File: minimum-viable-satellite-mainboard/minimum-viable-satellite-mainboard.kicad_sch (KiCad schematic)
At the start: 50 parts, among them J1 Breakout, J2 Breakout, Q1 FDMQ86530L, Q2 DMP2240UDM-7, Q3 DMP2240UDM-7, U1 TLV1704

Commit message: More Schematic Capture
- Moved WDT to its own sheet
- Added Solar Charger
- Added MCP Temp Sensor
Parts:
- removed C1, C2, C3, C4, C5: 10u, Capacitor_SMD:C_0603_1608Metric, symbol Device:C_Small
- removed D1, D3: 1N4151WS, Diode_SMD:D_SOD-323, symbol oresat-diodes:1N4151WS-HE3
- removed D2: GREEN, LED_SMD:LED_0603_1608Metric, symbol Device:LED_Small_Filled
- removed J1: Breakout, Connector_PinHeader_2.54mm:PinHeader_1x04_P2.54mm_Vertical, symbol Connector_Generic:Conn_01x04
- removed J2: Breakout, FC_DEV_BOARD:JST_BM04B-SRSS-TB(LF)(SN), symbol Connector_Generic:Conn_01x04
- removed JP1: SolderJumper_2_Open, Jumper:SolderJumper-2_P1.3mm_Open_RoundedPad1.0x1.5mm, symbol Jumper:SolderJumper_2_Open
- removed R1: 10 (1206), Resistor_SMD:R_1206_3216Metric, symbol Device:R_Small_US
- removed R10, R12: 1k, Resistor_SMD:R_0603_1608Metric, symbol Device:R_Small_US
- removed R11, R13, R14, R15, R17, R18: 100k, Resistor_SMD:R_0603_1608Metric, symbol Device:R_Small_US
- removed R16: 4.7M, Resistor_SMD:R_0603_1608Metric, symbol Device:R_Small_US
- removed R2, R3, R4, R8, R9: 10k, Resistor_SMD:R_0603_1608Metric, symbol Device:R_Small_US
- removed R5, R6, R7: 3.0k, Resistor_SMD:R_0603_1608Metric, symbol Device:R_Small_US
- removed TP1, TP2, TP3, TP4, TP5, TP6: TestPoint-MinTH, oresat-misc:TestPoint-0.75mm-th, symbol oresat-misc:Test-Point-0.75mm-th
- removed U1: TLV1704, Package_SO:TSSOP-14_4.4x5mm_P0.65mm, symbol oresat-ics:TLV1704AIPWR
- added C10, C8: 10uF, Capacitor_SMD:C_0603_1608Metric, symbol mainboard:10UF-0603-6.3V-20%
- added C6, C7: 0.1uF, Capacitor_SMD:C_0603_1608Metric, symbol Device:C_Small
- added C9: 1uF, Capacitor_SMD:C_0603_1608Metric, symbol mainboard:10UF-0603-6.3V-20%
- added D10, D8: DFLS130L, Diode_SMD:D_PowerDI-123, symbol Device:D_Schottky
- added D5, D6, D7, D9: DFLS130L-7, Diode_SMD:D_PowerDI-123, symbol Device:D_Schottky
- added IC1: LT3652IMSE#PBF, Package_SO:MSOP-12-1EP_3x4mm_P0.65mm_EP1.65x2.85mm, symbol LT3652IMSE#PBF:LT3652IMSE#PBF
- added J3: Foot0, Battery Board:MOLEX_504050-0291, symbol Connector_Generic:Conn_01x02
- added J4: Foot1, Battery Board:MOLEX_504050-0291, symbol Connector_Generic:Conn_01x02
- added J5, J9: ISS Foot0, Battery Board:MOLEX_504050-0291, symbol Connector_Generic:Conn_01x02
- added J6: Foot2, Battery Board:MOLEX_504050-0291, symbol Connector_Generic:Conn_01x02
- added J7: Foot3, Battery Board:MOLEX_504050-0291, symbol Connector_Generic:Conn_01x02
- added J8: RBF Pin, Battery Board:MOLEX_504050-0291, symbol Connector_Generic:Conn_01x04
- added L1: 10uH, Inductor_SMD:L_1812_4532Metric, symbol Device:L
- added R25, R26, R35, R36: 0.002, Resistor_SMD:R_2512_6332Metric, symbol mainboard:R-US_R2512
- added R27: 100K, Resistor_SMD:R_0603_1608Metric, symbol Device:R_US
- added R28: 100k, Resistor_SMD:R_0603_1608Metric, symbol mainboard:R-US_R0603
- added R29: 94k, Resistor_SMD:R_0603_1608Metric, symbol mainboard:R-US_R0603
- added R30, R34: 10K, Resistor_SMD:R_0603_1608Metric, symbol Device:R_US
- added R31: 634k, Resistor_SMD:R_0603_1608Metric, symbol mainboard:R-US_R0603
- added R32: 412k, Resistor_SMD:R_0603_1608Metric, symbol mainboard:R-US_R0603
- added R33: 0.1, Resistor_SMD:R_2512_6332Metric, symbol mainboard:R-US_R0603
- added U2, U3: INA219AxD, Package_SO:SOIC-8_3.9x4.9mm_P1.27mm, symbol Analog_ADC:INA219AxD
- added U4: MCP9808_MSOP, Package_SO:MSOP-8_3x3mm_P0.65mm, symbol Sensor_Temperature:MCP9808_MSOP
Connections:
- net GND: now also C10.2, C6.1, C7.1, C8.2, D9.2 (A), IC1.13 (EP), IC1.6 (TIMER), J5.1 (Pin_1), J9.1 (Pin_1), R29.1, R32.1, R35.1, R36.1, U2.2 (A0), U2.6 (GND), U3.1 (A1), U3.2 (A0), U3.6 (GND), U4.4 (GND)
- new net: IC1.2 (VIN_REG), R28.2, R29.2
- new net: C8.1, D5.1 (K), D6.1 (K), IC1.1 (VIN), IC1.3 (~{SHDN}), R27.1
- new net: R27.2, R28.1
- new net: J6.1 (Pin_1), J7.2 (Pin_2)
- new net: C9.1, D9.1 (K), IC1.12 (SW), L1.1
- new net: C9.2, D8.1 (K), IC1.11 (BOOST)
- new net: J3.1 (Pin_1), J4.2 (Pin_2)
- new net: IC1.10 (SENSE), L1.2, R33.2
- new net: IC1.7 (VFB), R31.1, R32.2
- new net +3V3: C6.2, C7.2, R30.1, R34.1, U2.1 (A1), U2.5 (VS), U3.5 (VS), U4.8 (V_{DD})
- new net Dir_Chrg_In: D6.2 (A), D7.2 (A)
- new net PACK+: R26.2, U3.8 (IN+)
- new net PACK-: J5.2 (Pin_2), J9.2 (Pin_2), R35.2, R36.2
- new net SCL0: U2.4 (SCL), U3.4 (SCL)
- new net SDA0: U2.3 (SDA), U3.3 (SDA)
- new net VBATT_SENSE: C10.1, D10.2 (A), D8.2 (A), IC1.9 (BAT), R26.1, R31.2, R33.1, U3.7 (IN-)
- new net VBUSP: J8.1 (Pin_1), J8.2 (Pin_2)
- new net VBatt: D10.1 (K), D7.1 (K), J3.2 (Pin_2), J6.2 (Pin_2)
- new net VBatt1: J4.1 (Pin_1), J7.1 (Pin_1), J8.3 (Pin_3), J8.4 (Pin_4)
- new net VSOLAR_IN: D5.2 (A), R25.2, U2.8 (IN+)
- new net VSOLAR_OUT: R25.1, U2.7 (IN-)
- new net ~{CHRG}: IC1.4 (~{CHRG}), R30.2
- new net ~{FAULT}: IC1.5 (~{FAULT}), R34.2
- no-connect marks 4 -> 5
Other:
- added sheet Watchdog Timer (watchdog.kicad_sch)
- note added: "2S Li-Ion Battery Solar Charging Circuit"
- note added: "Battery Power Monitor"
- note added: "Current Sense Resistor: 2mOhm suggested on datasheet"
- note added: "Schottky Diode"
- note added: "Solar Power Monitor"
- note added: "Temperature Sensor"
- note added: "VSOLAR 9V to 40V"
- note removed: "C112+C114 and R62+R63 set the WDT frequency"
- note removed: "DC block and pulse detector"
- note removed: "Disable shutdown during initial power up."
- note removed: "OreSat Watch-Dog Timer"
- note removed: "Oscillator"
- note removed: "Output buffer"
- note removed: "Pull-up on battery pack to Vbus"
- note removed: "Pulse integrator"
- note removed: "TLV1704AMPWPSEP is the radiation tolerant version. Use TLV1704AQPWRQ1 for non-flight C3 boards."
- note removed: "WDT enabled when soldered"
- note removed: "~ 24 s period (36 s on power up)"
- moved on the sheet: D4, Q1, Q2A, Q2B, Q3A, Q3B, R19, R20, R21, R22, R23, R24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

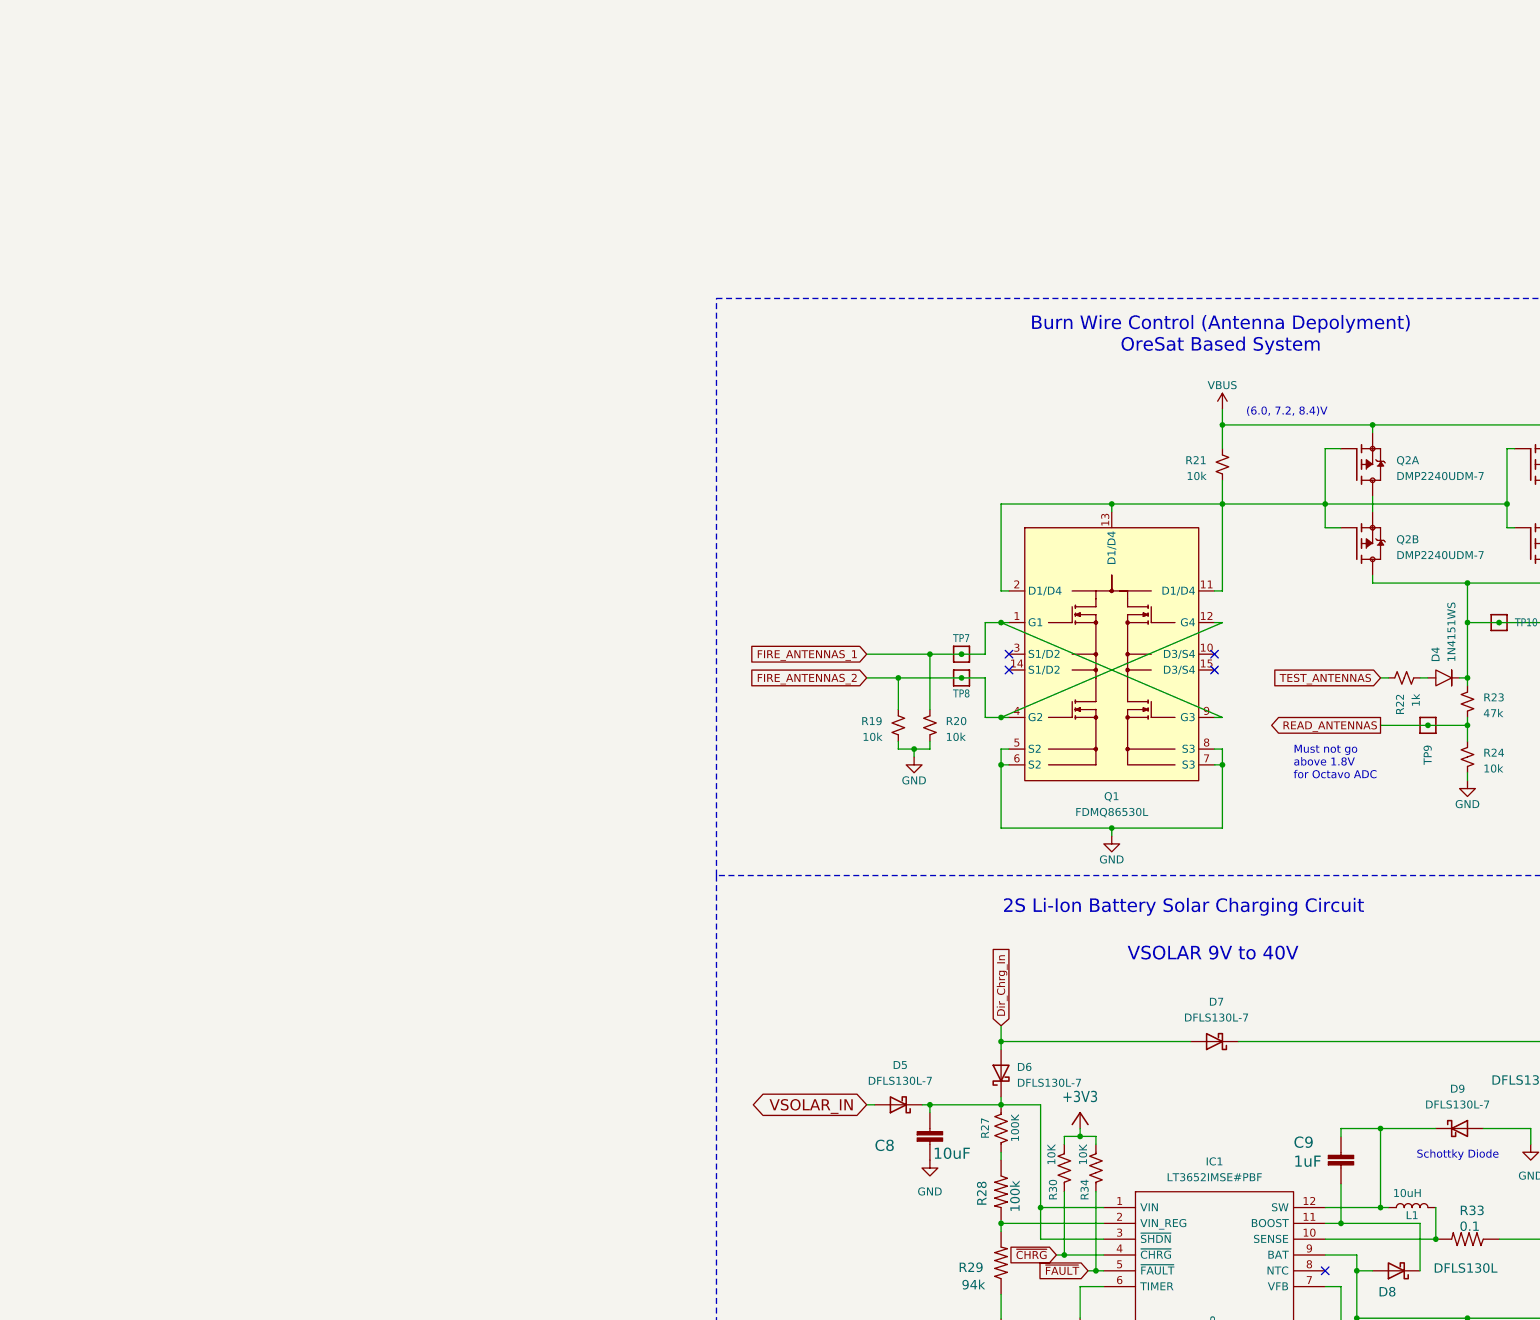
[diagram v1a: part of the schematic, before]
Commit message: added MSP430
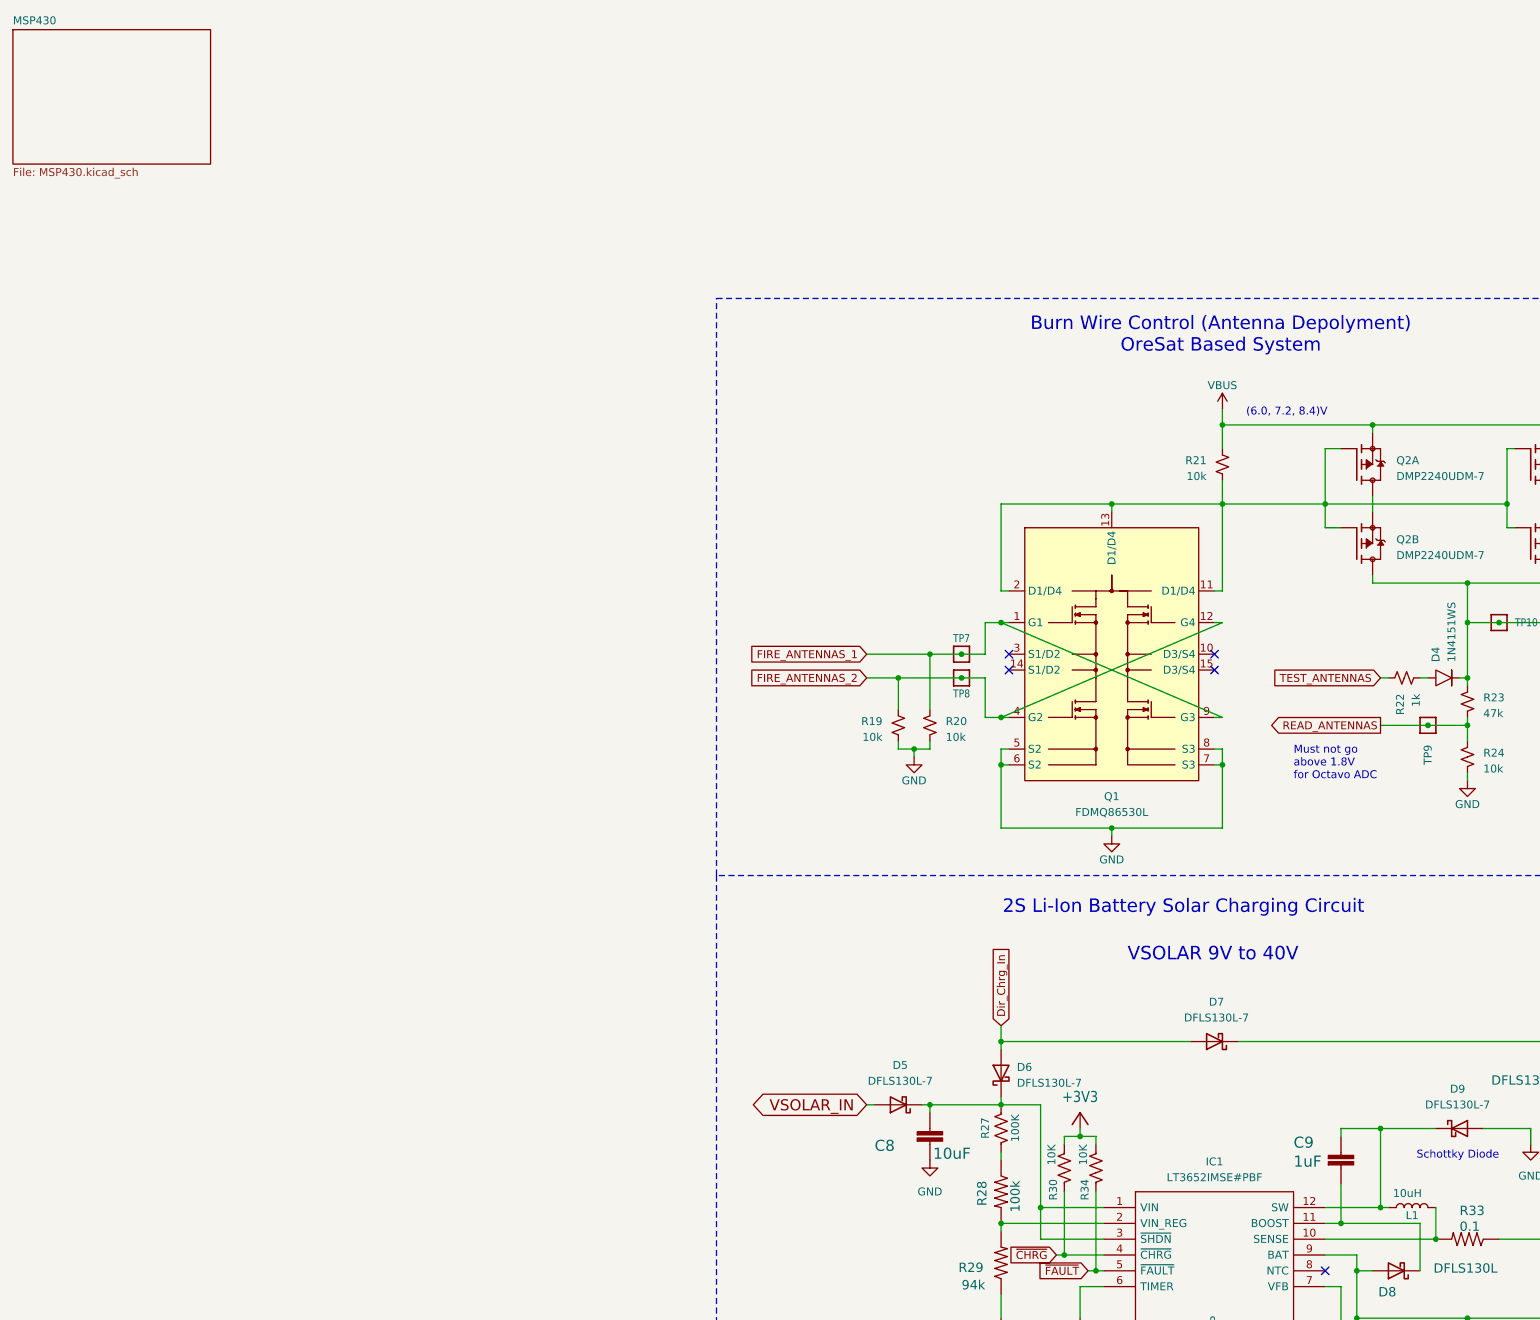
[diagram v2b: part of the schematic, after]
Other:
- added sheet MSP430 (MSP430.kicad_sch)
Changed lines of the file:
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@@
 (kicad_sch
-	(version 20231120)
+	(version 20250114)
 	(generator "eeschema")
-	(generator_version "8.0")
+	(generator_version "9.0")
 	(paper "A3")
+	(text "2S Li-Ion Battery Solar Charging Circuit"
+		(exclude_from_sim no)
+		(at 179.324 161.29 0)
+		(effects
+			(font
+				(size 2.159 2.159)
+			)
+			(justify left bottom)
+		)
+	)
+	(text "Current Sense Resistor:\n2mOhm suggested on datasheet\n"
+		(exclude_from_sim no)
+		(at 311.15 181.61 0)
+		(effects
+			(font
+				(size 0.889 0.889)
+			)
+			(justify left bottom)
+		)
+	)
+	(text "Current Sense Resistor:\n2mOhm suggested on datasheet\n"
+		(exclude_from_sim no)
+		(at 313.69 221.488 0)
+		(effects
+			(font
+				(size 0.889 0.889)
+			)
+			(justify left bottom)
+		)
+	)
+	(text "Must not go \nabove 1.8V \nfor Octavo ADC"
+		(exclude_from_sim no)
+		(at 226.06 139.7 0)
+		(effects
+			(font
+				(size 1.27 1.27)
+			)
+			(justify left bottom)
+		)
+	)
+	(text "Battery Power Monitor"
+		(exclude_from_sim no)
+		(at 349.25 206.248 0)
+		(effects
+			(font
+				(size 2.159 2.159)
+			)
+			(justify left bottom)
+		)
+	)
+	(text "Schottky Diode\n"
+		(exclude_from_sim no)
+		(at 259.08 200.66 0)
+		(effects
+			(font
+				(size 1.27 1.27)
+			)
+			(justify right bottom)
+		)
+	)
+	(text "VSOLAR 9V to 40V"
+		(exclude_from_sim no)
+		(at 199.39 168.91 0)
+		(effects
+			(font
+				(size 2.159 2.159)
+			)
+			(justify left bottom)
+		)
+	)
+	(text "Solar Power Monitor"
+		(exclude_from_sim no)
+		(at 346.71 165.608 0)
+		(effects
+			(font
+				(size 2.159 2.159)
+			)
+			(justify left bottom)
+		)
+	)
+	(text "Burn Wire Control (Antenna Depolyment)\nOreSat Based System"
+		(exclude_from_sim no)
+		(at 214.376 71.12 0)
+		(effects
+			(font
+				(size 2.159 2.159)
+			)
+			(justify bottom)
+		)
+	)
+	(text "(6.0, 7.2, 8.4)V"
+		(exclude_from_sim no)
+		(at 218.44 81.28 0)
+		(effects
+			(font
+				(size 1.27 1.27)
+			)
+			(justify left bottom)
+		)
+	)
+	(text "Temperature Sensor\n"
+		(exclude_from_sim no)
+		(at 357.124 83.312 0)
+		(effects
+			(font
+				(size 1.27 1.27)
+			)
+		)
+	)
 	(junction
 		(at 167.64 191.77)
@@
 		)
 	)
-	(text "2S Li-Ion Battery Solar Charging Circuit"
-		(exclude_from_sim no)
-		(at 179.324 161.29 0)
-		(effects
-			(font
-				(size 2.159 2.159)
-			)
-			(justify left bottom)
-		)
-	)
-	(text "Current Sense Resistor:\n2mOhm suggested on datasheet\n"
-		(exclude_from_sim no)
-		(at 311.15 181.61 0)
-		(effects
-			(font
-				(size 0.889 0.889)
-			)
-			(justify left bottom)
-		)
-	)
-	(text "Current Sense Resistor:\n2mOhm suggested on datasheet\n"
-		(exclude_from_sim no)
-		(at 313.69 221.488 0)
-		(effects
-			(font
-				(size 0.889 0.889)
-			)
-			(justify left bottom)
-		)
-	)
-	(text "Must not go \nabove 1.8V \nfor Octavo ADC"
-		(exclude_from_sim no)
-		(at 226.06 139.7 0)
-		(effects
-			(font
-				(size 1.27 1.27)
-			)
-			(justify left bottom)
-		)
-	)
-	(text "Battery Power Monitor"
-		(exclude_from_sim no)
-		(at 349.25 206.248 0)
-		(effects
-			(font
-				(size 2.159 2.159)
-			)
-			(justify left bottom)
-		)
-	)
-	(text "Schottky Diode\n"
-		(exclude_from_sim no)
-		(at 259.08 200.66 0)
-		(effects
-			(font
-				(size 1.27 1.27)
-			)
-			(justify right bottom)
-		)
-	)
-	(text "VSOLAR 9V to 40V"
-		(exclude_from_sim no)
-		(at 199.39 168.91 0)
-		(effects
-			(font
-				(size 2.159 2.159)
-			)
-			(justify left bottom)
-		)
-	)
-	(text "Solar Power Monitor"
-		(exclude_from_sim no)
-		(at 346.71 165.608 0)
-		(effects
-			(font
-				(size 2.159 2.159)
-			)
-			(justify left bottom)
-		)
-	)
-	(text "Burn Wire Control (Antenna Depolyment)\nOreSat Based System"
-		(exclude_from_sim no)
-		(at 214.376 71.12 0)
-		(effects
-			(font
-				(size 2.159 2.159)
-			)
-			(justify bottom)
-		)
-	)
-	(text "(6.0, 7.2, 8.4)V"
-		(exclude_from_sim no)
-		(at 218.44 81.28 0)
-		(effects
-			(font
-				(size 1.27 1.27)
-			)
-			(justify left bottom)
-		)
-	)
-	(text "Temperature Sensor\n"
-		(exclude_from_sim no)
-		(at 357.124 83.312 0)
-		(effects
-			(font
-				(size 1.27 1.27)
-			)
-		)
-	)
 	(global_label "GND"
 		(shape bidirectional)
@@
 		(at 261.62 261.62)
 		(size 29.21 15.24)
+		(exclude_from_sim no)
+		(in_bom yes)
+		(on_board yes)
+		(dnp no)
 		(fields_autoplaced yes)
 		(stroke
@@
 		)
 	)
+	(sheet
+		(at 20.32 19.05)
+		(size 31.75 21.59)
+		(exclude_from_sim no)
+		(in_bom yes)
+		(on_board yes)
+		(dnp no)
+		(fields_autoplaced yes)
+		(stroke
+			(width 0.1524)
+			(type solid)
+		)
+		(fill
+			(color 0 0 0 0.0000)
+		)
+		(property "Sheetname" "MSP430"
+			(at 20.32 18.3384 0)
+			(effects
+				(font
+					(size 1.27 1.27)
+				)
+				(justify left bottom)
+			)
+		)
+		(property "Sheetfile" "MSP430.kicad_sch"
+			(at 20.32 41.2246 0)
+			(effects
+				(font
+					(size 1.27 1.27)
+				)
+				(justify left top)
+			)
+		)
+		(instances
+			(project "minimum-viable-satellite-mainboard"
+				(path "/574aef03-50c0-457b-ac4e-eeea858fe9e9"
+					(page "3")
+				)
+			)
+		)
+	)
 	(sheet_instances
 		(path "/"
@@
 		)
 	)
+	(embedded_fonts no)
 )
